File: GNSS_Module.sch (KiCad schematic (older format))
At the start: 10 parts, among them J12 GPS Shield, J13 GPS_Trasnmission_Conn, U9 ublox_SAM-M8Q

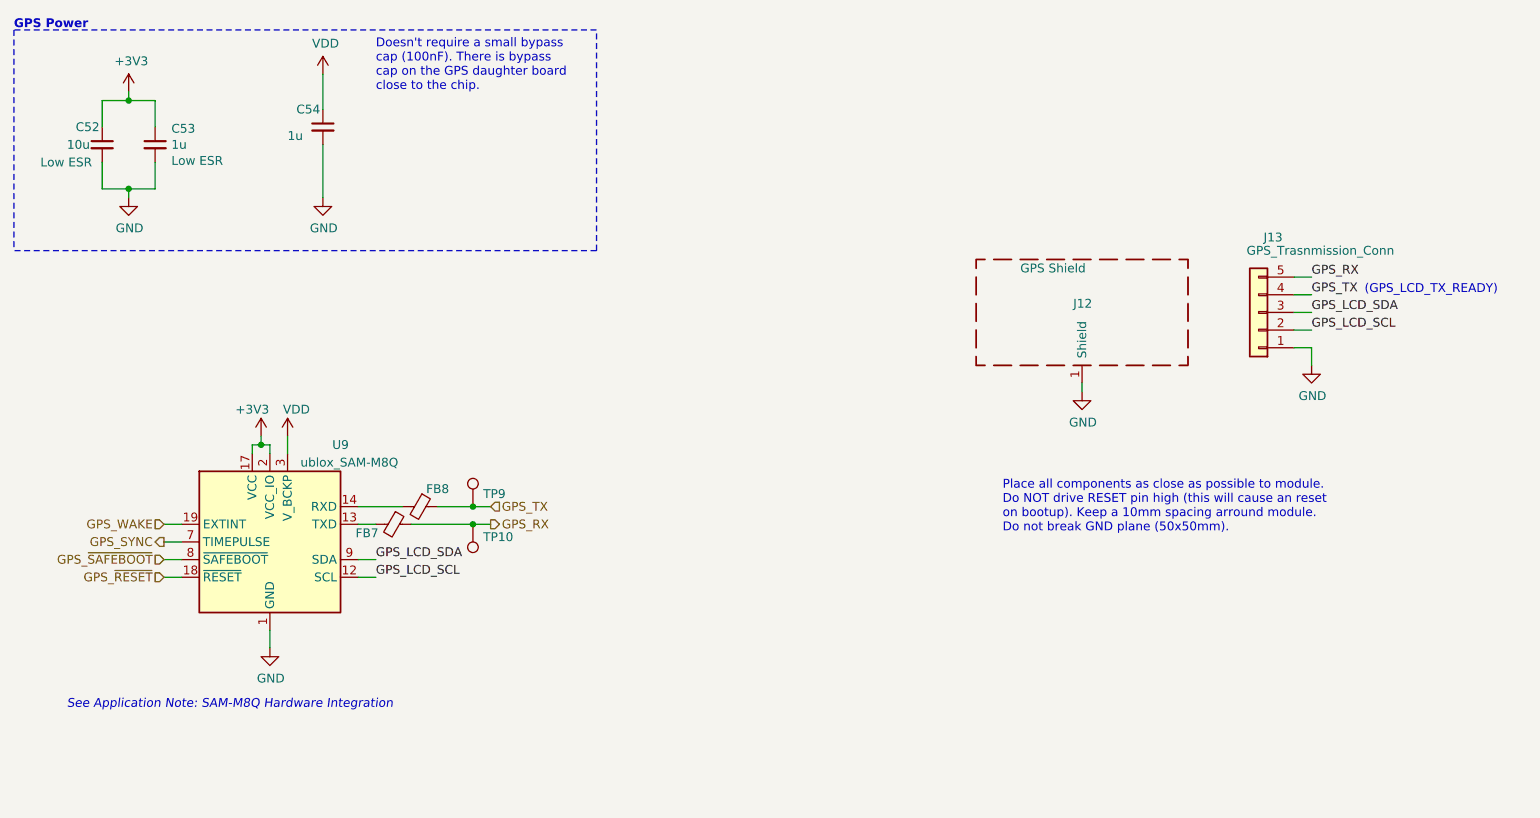
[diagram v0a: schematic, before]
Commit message: Change voltage polarity diode
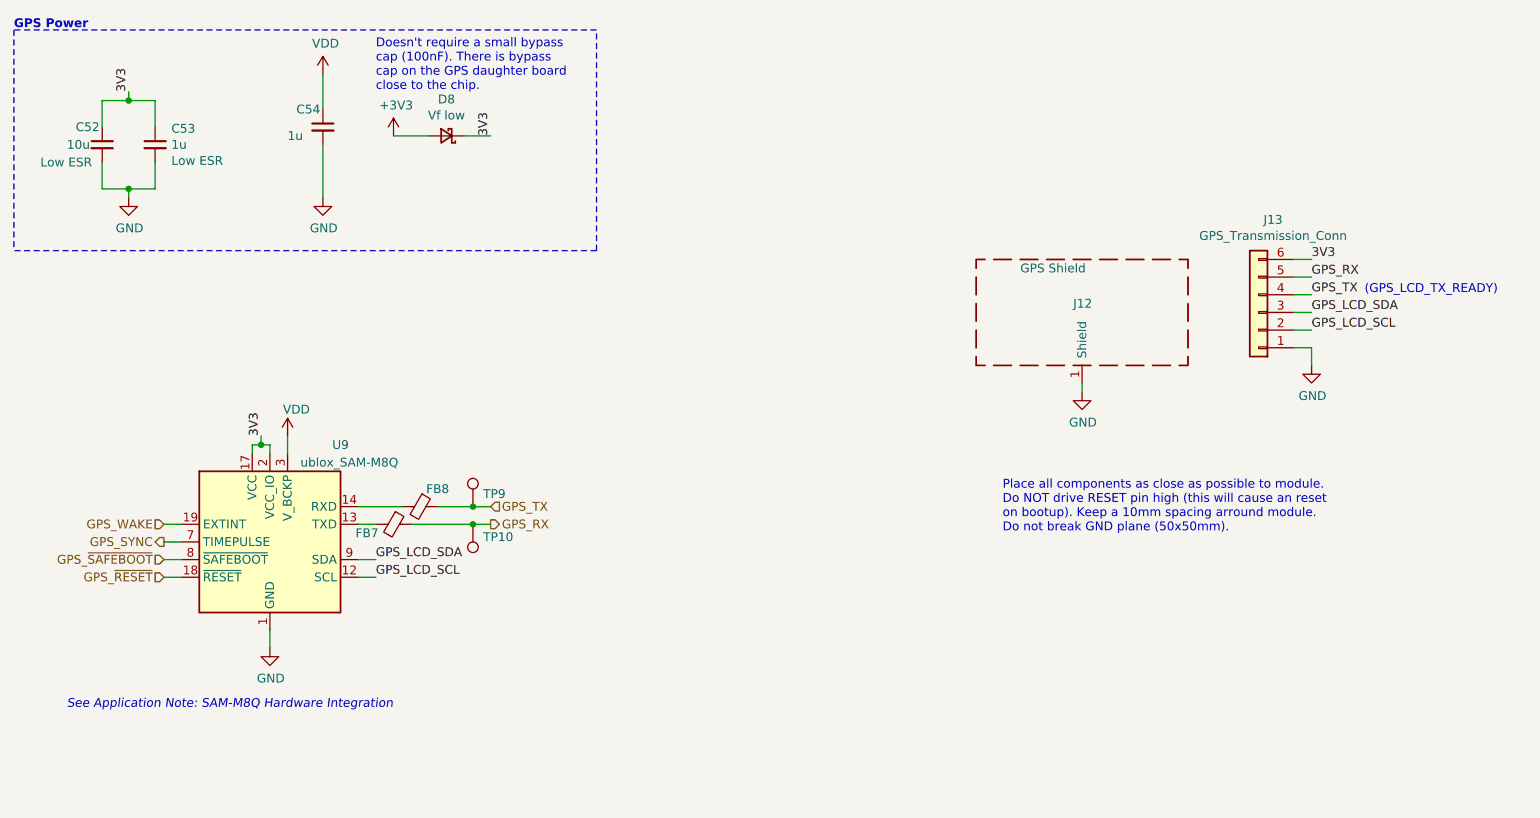
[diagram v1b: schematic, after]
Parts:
- removed J13: GPS_Trasnmission_Conn, Connector_PinHeader_2.54mm:PinHeader_1x05_P2.54mm_Vertical, symbol Connector_Generic:Conn_01x05
- added D8: Vf low, Diode_SMD:D_SOD-123, symbol Device:D_Schottky_Small
- added J13: GPS_Transmission_Conn, Connector_PinHeader_2.54mm:PinHeader_1x06_P2.54mm_Vertical, symbol Connector_Generic:Conn_01x06
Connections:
- net +3V3: now also D8.2 (A); no longer C52.1, C53.1, U9.17 (VCC), U9.2 (VCC_IO)
- net GND: now also J13.1 (Pin_1)
- net GPS_LCD_SCL: now also J13.2 (Pin_2)
- net GPS_LCD_SDA: now also J13.3 (Pin_3)
- net GPS_RX: now also J13.5 (Pin_5)
- net GPS_TX: now also J13.4 (Pin_4)
- new net 3V3: C52.1, C53.1, D8.1 (K), J13.6 (Pin_6), U9.17 (VCC), U9.2 (VCC_IO)
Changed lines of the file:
@@
 	2250 1750 2100 1750
-$Comp
-L power:+3V3 #PWR?
-U 1 1 5EE05208
-P 2250 1200
-AR Path="/5EE05208" Ref="#PWR?"  Part="1"
-AR Path="/5EDF3693/5EE05208" Ref="#PWR0120"  Part="1"
-F 0 "#PWR0120" H 2250 1050 50  0001 C CNN
-F 1 "+3V3" H 2265 1373 50  0000 C CNN
-F 2 "" H 2250 1200 50  0001 C CNN
-F 3 "" H 2250 1200 50  0001 C CNN
-	1    2250 1200
-	1    0    0    -1
-$EndComp
 $Comp
 L power:GND #PWR?
@@
 F 3 "" H 3350 1800 50  0001 C CNN
 	1    3350 1800
-	1    0    0    -1
-$EndComp
-$Comp
-L power:+3V3 #PWR?
-U 1 1 5EE05214
-P 3000 3150
-AR Path="/5EE05214" Ref="#PWR?"  Part="1"
-AR Path="/5EDF3693/5EE05214" Ref="#PWR0122"  Part="1"
-F 0 "#PWR0122" H 3000 3000 50  0001 C CNN
-F 1 "+3V3" H 2950 3300 50  0000 C CNN
-F 2 "" H 3000 3150 50  0001 C CNN
-F 3 "" H 3000 3150 50  0001 C CNN
-	1    3000 3150
 	1    0    0    -1
 $EndComp
@@
 Wire Wire Line
 	3550 3950 3650 3950
-$Comp
-L Connector_Generic:Conn_01x05 J?
-U 1 1 5EE05249
-P 8650 2450
-AR Path="/5EE05249" Ref="J?"  Part="1"
-AR Path="/5EDF3693/5EE05249" Ref="J13"  Part="1"
-F 0 "J13" H 8568 2025 50  0000 C CNN
-F 1 "GPS_Trasnmission_Conn" H 8300 2100 50  0000 C CNN
-F 2 "Connector_PinHeader_2.54mm:PinHeader_1x05_P2.54mm_Vertical" H 8650 2450 50  0001 C CNN
-F 3 "~" H 8650 2450 50  0001 C CNN
-	1    8650 2450
-	-1   0    0    1
-$EndComp
 $Comp
 L power:GND #PWR?
@@
 Wire Wire Line
 	3350 1100 3350 1300
+$Comp
+L Connector_Generic:Conn_01x06 J13
+U 1 1 5EEF6B4C
+P 8650 2450
+F 0 "J13" H 8568 1925 50  0000 C CNN
+F 1 "GPS_Transmission_Conn" H 8568 2016 50  0000 C CNN
+F 2 "Connector_PinHeader_2.54mm:PinHeader_1x06_P2.54mm_Vertical" H 8650 2450 50  0001 C CNN
+F 3 "~" H 8650 2450 50  0001 C CNN
+	1    8650 2450
+	-1   0    0    1
+$EndComp
+Text Label 8950 2150 0    50   ~ 0
+3V3
+Wire Wire Line
+	8950 2150 8850 2150
+Text Label 2250 1200 1    50   ~ 0
+3V3
+Text Label 3000 3150 1    50   ~ 0
+3V3
+Wire Wire Line
+	3950 1450 3750 1450
+Wire Wire Line
+	4300 1450 4150 1450
+Text Label 4300 1450 1    50   ~ 0
+3V3
+$Comp
+L power:+3V3 #PWR0120
+U 1 1 5EF0BA19
+P 3750 1450
+F 0 "#PWR0120" H 3750 1300 50  0001 C CNN
+F 1 "+3V3" H 3765 1623 50  0000 C CNN
+F 2 "" H 3750 1450 50  0001 C CNN
+F 3 "" H 3750 1450 50  0001 C CNN
+	1    3750 1450
+	1    0    0    -1
+$EndComp
+$Comp
+L Device:D_Schottky_Small D?
+U 1 1 5EF05AAC
+P 4050 1450
+AR Path="/5EEDE770/5EF05AAC" Ref="D?"  Part="1"
+AR Path="/5EDF3693/5EF05AAC" Ref="D8"  Part="1"
+F 0 "D8" H 4050 1243 50  0000 C CNN
+F 1 "Vf low" H 4050 1334 50  0000 C CNN
+F 2 "Diode_SMD:D_SOD-123" V 4050 1450 50  0001 C CNN
+F 3 "~" V 4050 1450 50  0001 C CNN
+F 4 "RSX101MM-30TR" H 4050 1450 50  0001 C CNN "MPN"
+F 5 "ROHM Semiconductor" H 4050 1450 50  0001 C CNN "Mfr."
+	1    4050 1450
+	-1   0    0    1
+$EndComp
 $EndSCHEMATC

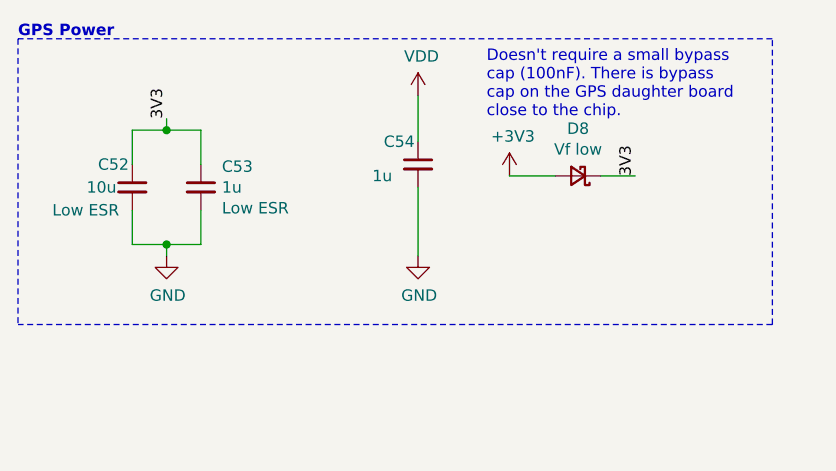
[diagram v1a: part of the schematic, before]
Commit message: Change Mic Preamp
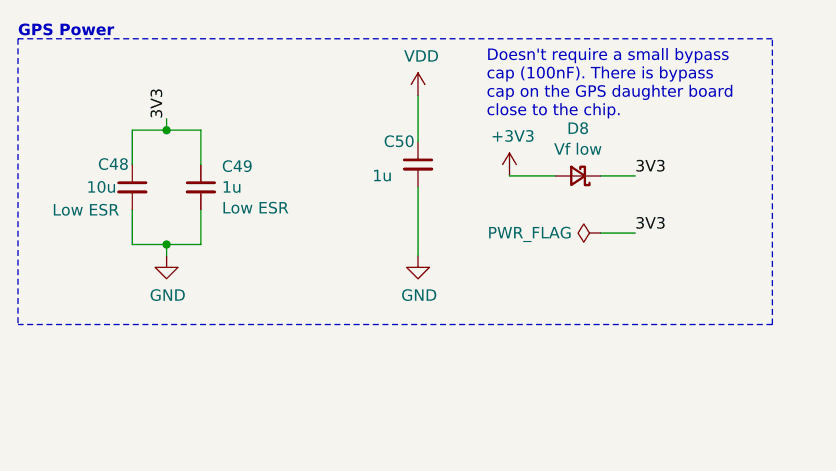
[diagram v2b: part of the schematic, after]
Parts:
- C48: renamed from C52; MPN (none) -> C0805C106K9PACTU; Mfr. (none) -> KEMET
- C50: renamed from C54; MPN (none) -> C0603C105K8RACTU; Mfr. (none) -> KEMET
- FB7, FB8: MPN BLM15HD102SN1 -> BLM15HD102SN1D; Mfr. (none) -> Murata Electronics
- renumbered C53 to C49
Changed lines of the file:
@@
 P 2250 1800
 AR Path="/5EE05200" Ref="#PWR?"  Part="1"
-AR Path="/5EDF3693/5EE05200" Ref="#PWR0121"  Part="1"
-F 0 "#PWR0121" H 2250 1550 50  0001 C CNN
+AR Path="/5EDF3693/5EE05200" Ref="#PWR0128"  Part="1"
+F 0 "#PWR0128" H 2250 1550 50  0001 C CNN
 F 1 "GND" H 2255 1627 50  0000 C CNN
 F 2 "" H 2250 1800 50  0001 C CNN
@@
 P 3350 1800
 AR Path="/5EE0520E" Ref="#PWR?"  Part="1"
-AR Path="/5EDF3693/5EE0520E" Ref="#PWR0126"  Part="1"
-F 0 "#PWR0126" H 3350 1550 50  0001 C CNN
+AR Path="/5EDF3693/5EE0520E" Ref="#PWR0132"  Part="1"
+F 0 "#PWR0132" H 3350 1550 50  0001 C CNN
 F 1 "GND" H 3355 1627 50  0000 C CNN
 F 2 "" H 3350 1800 50  0001 C CNN
@@
 P 3050 4350
 AR Path="/5EE05234" Ref="#PWR?"  Part="1"
-AR Path="/5EDF3693/5EE05234" Ref="#PWR0123"  Part="1"
-F 0 "#PWR0123" H 3050 4100 50  0001 C CNN
+AR Path="/5EDF3693/5EE05234" Ref="#PWR0129"  Part="1"
+F 0 "#PWR0129" H 3050 4100 50  0001 C CNN
 F 1 "GND" H 3055 4177 50  0000 C CNN
 F 2 "" H 3050 4350 50  0001 C CNN
@@
 F 2 "Inductor_SMD:L_0402_1005Metric" V 3680 3650 50  0001 C CNN
 F 3 "~" H 3750 3650 50  0001 C CNN
-F 4 "BLM15HD102SN1" V 3750 3650 50  0001 C CNN "MPN"
+F 4 "BLM15HD102SN1D" V 3750 3650 50  0001 C CNN "MPN"
+F 5 "Murata Electronics" H 3750 3650 50  0001 C CNN "Mfr."
 	1    3750 3650
 	0    1    1    0
@@
 P 8950 2750
 AR Path="/5EE0524F" Ref="#PWR?"  Part="1"
-AR Path="/5EDF3693/5EE0524F" Ref="#PWR0128"  Part="1"
-F 0 "#PWR0128" H 8950 2500 50  0001 C CNN
+AR Path="/5EDF3693/5EE0524F" Ref="#PWR0135"  Part="1"
+F 0 "#PWR0135" H 8950 2500 50  0001 C CNN
 F 1 "GND" H 8955 2577 50  0000 C CNN
 F 2 "" H 8950 2750 50  0001 C CNN
@@
 P 2400 1500
 AR Path="/5EE0527F" Ref="C?"  Part="1"
-AR Path="/5EDF3693/5EE0527F" Ref="C53"  Part="1"
-F 0 "C53" H 2492 1591 50  0000 L CNN
+AR Path="/5EDF3693/5EE0527F" Ref="C49"  Part="1"
+F 0 "C49" H 2492 1591 50  0000 L CNN
 F 1 "1u" H 2492 1500 50  0000 L CNN
 F 2 "Capacitor_SMD:C_0603_1608Metric_Pad1.05x0.95mm_HandSolder" H 2400 1500 50  0001 C CNN
@@
 P 3350 1400
 AR Path="/5EE05285" Ref="C?"  Part="1"
-AR Path="/5EDF3693/5EE05285" Ref="C54"  Part="1"
-F 0 "C54" H 3200 1500 50  0000 L CNN
+AR Path="/5EDF3693/5EE05285" Ref="C50"  Part="1"
+F 0 "C50" H 3200 1500 50  0000 L CNN
 F 1 "1u" H 3150 1350 50  0000 L CNN
 F 2 "Capacitor_SMD:C_0603_1608Metric_Pad1.05x0.95mm_HandSolder" H 3350 1400 50  0001 C CNN
 F 3 "~" H 3350 1400 50  0001 C CNN
+F 4 "C0603C105K8RACTU" H 3350 1400 50  0001 C CNN "MPN"
+F 5 "KEMET" H 3350 1400 50  0001 C CNN "Mfr."
 	1    3350 1400
 	1    0    0    -1
@@
 P 2100 1500
 AR Path="/5EE0528E" Ref="C?"  Part="1"
-AR Path="/5EDF3693/5EE0528E" Ref="C52"  Part="1"
-F 0 "C52" H 1950 1600 50  0000 L CNN
+AR Path="/5EDF3693/5EE0528E" Ref="C48"  Part="1"
+F 0 "C48" H 1950 1600 50  0000 L CNN
 F 1 "10u" H 1900 1500 50  0000 L CNN
 F 2 "Capacitor_SMD:C_0805_2012Metric_Pad1.15x1.40mm_HandSolder" H 2100 1500 50  0001 C CNN
 F 3 "~" H 2100 1500 50  0001 C CNN
 F 4 "Low ESR" H 1750 1400 50  0000 L CNN "Notes"
+F 5 "C0805C106K9PACTU" H 2100 1500 50  0001 C CNN "MPN"
+F 6 "KEMET" H 2100 1500 50  0001 C CNN "Mfr."
 	1    2100 1500
 	1    0    0    -1
@@
 P 7650 2900
 AR Path="/5EE052A0" Ref="#PWR?"  Part="1"
-AR Path="/5EDF3693/5EE052A0" Ref="#PWR0127"  Part="1"
-F 0 "#PWR0127" H 7650 2650 50  0001 C CNN
+AR Path="/5EDF3693/5EE052A0" Ref="#PWR0134"  Part="1"
+F 0 "#PWR0134" H 7650 2650 50  0001 C CNN
 F 1 "GND" H 7655 2727 50  0000 C CNN
 F 2 "" H 7650 2900 50  0001 C CNN
@@
 P 3350 1100
 AR Path="/5EE052A8" Ref="#PWR?"  Part="1"
-AR Path="/5EDF3693/5EE052A8" Ref="#PWR0125"  Part="1"
-F 0 "#PWR0125" H 3350 950 50  0001 C CNN
+AR Path="/5EDF3693/5EE052A8" Ref="#PWR0131"  Part="1"
+F 0 "#PWR0131" H 3350 950 50  0001 C CNN
 F 1 "VDD" H 3365 1273 50  0000 C CNN
 F 2 "" H 3350 1100 50  0001 C CNN
@@
 P 3150 3150
 AR Path="/5EE052B2" Ref="#PWR?"  Part="1"
-AR Path="/5EDF3693/5EE052B2" Ref="#PWR0124"  Part="1"
-F 0 "#PWR0124" H 3150 3000 50  0001 C CNN
+AR Path="/5EDF3693/5EE052B2" Ref="#PWR0130"  Part="1"
+F 0 "#PWR0130" H 3150 3000 50  0001 C CNN
 F 1 "VDD" H 3200 3300 50  0000 C CNN
 F 2 "" H 3150 3150 50  0001 C CNN
@@
 F 2 "Inductor_SMD:L_0402_1005Metric" V 3830 3550 50  0001 C CNN
 F 3 "~" H 3900 3550 50  0001 C CNN
-F 4 "BLM15HD102SN1" V 3900 3550 50  0001 C CNN "MPN"
+F 4 "BLM15HD102SN1D" V 3900 3550 50  0001 C CNN "MPN"
+F 5 "Murata Electronics" H 3900 3550 50  0001 C CNN "Mfr."
 	1    3900 3550
 	0    1    1    0
@@
 Wire Wire Line
 	4300 1450 4150 1450
-Text Label 4300 1450 1    50   ~ 0
-3V3
-$Comp
-L power:+3V3 #PWR0120
+Text Label 4300 1450 0    50   ~ 0
+3V3
+$Comp
+L power:+3V3 #PWR0133
 U 1 1 5EF0BA19
 P 3750 1450
-F 0 "#PWR0120" H 3750 1300 50  0001 C CNN
+F 0 "#PWR0133" H 3750 1300 50  0001 C CNN
 F 1 "+3V3" H 3765 1623 50  0000 C CNN
 F 2 "" H 3750 1450 50  0001 C CNN
@@
 	-1   0    0    1
 $EndComp
+$Comp
+L power:PWR_FLAG #FLG010
+U 1 1 5EF35E8F
+P 4150 1700
+F 0 "#FLG010" H 4150 1775 50  0001 C CNN
+F 1 "PWR_FLAG" V 4150 1827 50  0000 L CNN
+F 2 "" H 4150 1700 50  0001 C CNN
+F 3 "~" H 4150 1700 50  0001 C CNN
+	1    4150 1700
+	0    -1   -1   0
+$EndComp
+Text Label 4300 1700 0    50   ~ 0
+3V3
+Wire Wire Line
+	4300 1700 4150 1700
 $EndSCHEMATC

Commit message: Fix BOM ref
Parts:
- J13: MPN (none) -> M50-055023W0445; Mfr. (none) -> Harwin
- U9: MPN (none) -> SAM-M8Q; Mfr. (none) -> U-BLOX
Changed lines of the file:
@@
 $Descr A4 11693 8268
 encoding utf-8
-Sheet 15 15
+Sheet 17 17
 Title "Kleinvoet"
 Date "2020-06-11"
@@
 F 2 "RF_GPS:ublox_SAM-M8Q" H 3550 3300 50  0001 C CNN
 F 3 "https://www.u-blox.com/sites/default/files/SAM-M8Q_DataSheet_%28UBX-16012619%29.pdf" H 3050 3750 50  0001 C CNN
+F 4 "SAM-M8Q" H 3050 3750 50  0001 C CNN "MPN"
+F 5 "U-BLOX" H 3050 3750 50  0001 C CNN "Mfr."
 	1    3050 3750
 	1    0    0    -1
@@
 F 2 "Connector_PinHeader_2.54mm:PinHeader_1x06_P2.54mm_Vertical" H 8650 2450 50  0001 C CNN
 F 3 "~" H 8650 2450 50  0001 C CNN
+F 4 "M50-055023W0445" H 8650 2450 50  0001 C CNN "MPN"
+F 5 "Harwin" H 8650 2450 50  0001 C CNN "Mfr."
 	1    8650 2450
 	-1   0    0    1

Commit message: Change Sensor Connectors
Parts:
- J12: footprint RF_Shielding:Wuerth_36503505_50x50mm -> RF_Shielding:Wuerth_36103505_50x50mm
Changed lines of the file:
@@
 F 0 "J12" H 7600 2500 50  0000 L CNN
 F 1 "GPS Shield" H 7300 2700 50  0000 L CNN
-F 2 "RF_Shielding:Wuerth_36503505_50x50mm" H 7650 2350 50  0001 C CNN
+F 2 "RF_Shielding:Wuerth_36103505_50x50mm" H 7650 2350 50  0001 C CNN
 F 3 "~" H 7650 2350 50  0001 C CNN
 	1    7650 2450

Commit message: PCB Layout Checkpoint
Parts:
- removed D8: Vf low, Diode_SMD:D_SOD-123, symbol Device:D_Schottky_Small
- removed FB7: BLM15HD102SN1, Inductor_SMD:L_0402_1005Metric, symbol Device:Ferrite_Bead_Small
- removed TP10, TP9: TestPoint, TestPoint:TestPoint_Pad_D1.0mm, symbol Connector:TestPoint
- added CB40: 100n, Capacitor_SMD:C_0603_1608Metric_Pad1.05x0.95mm_HandSolder, symbol Device:C_Small
- U11: renamed from U9; footprint RF_GPS:ublox_SAM-M8Q -> grootvoet:ublox_SAM-M8Q_HandSolder
- renumbered C48 to C64, C49 to C65, C50 to C66, FB8 to FB10, J12 to J14, J13 to J15
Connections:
- net 3V3 is gone; now on net +3V3: C64.1, C65.1, J15.6 (Pin_6), U11.17 (VCC), U11.2 (VCC_IO)
- net GND: now also CB40.2
- net GPS_LCD_SCL: now also J15.4 (Pin_4); no longer J15.2 (Pin_2)
- net GPS_LCD_SDA: now also J15.5 (Pin_5); no longer J15.3 (Pin_3)
- net GPS_RX: now also J15.3 (Pin_3), U11.13 (TXD); no longer J15.5 (Pin_5)
- net GPS_TX: now also J15.2 (Pin_2); no longer J15.4 (Pin_4)
- net GPS_~RESET: now also CB40.1

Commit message: Major Commit with Final PCB Design
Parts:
- removed J14: GPS Shield, RF_Shielding:Wuerth_36103505_50x50mm, symbol Device:RF_Shield_One_Piece
- removed J15: GPS_Transmission_Conn, Connector_PinHeader_2.54mm:PinHeader_1x06_P2.54mm_Vertical, symbol Connector_Generic:Conn_01x06
- added D2: GREEN, LED_SMD:LED_0603_1608Metric_Pad1.05x0.95mm_HandSolder, symbol Device:LED_Small
- added D3: YELLOW, LED_SMD:LED_0603_1608Metric_Pad1.05x0.95mm_HandSolder, symbol Device:LED_Small
- added H13, H14, H15, H16: MountingHole_Pad, MountingHole:MountingHole_4.3mm_M4_Pad_Via, symbol Mechanical:MountingHole_Pad
- added J14: GPS_Transmission_Conn, Connector_PinHeader_1.27mm:PinHeader_1x08_P1.27mm_Vertical, symbol Connector_Generic:Conn_01x08
- added J16: GPS_Transmission_Conn, Connector_PinHeader_1.27mm:PinHeader_2x04_P1.27mm_Vertical, symbol Connector_Generic:Conn_02x04_Odd_Even
- added J2: FTDI_Conn, Connector_PinHeader_2.54mm:PinHeader_1x06_P2.54mm_Vertical, symbol Connector_Generic:Conn_01x06
- added R3, R4: 2.2k, Resistor_SMD:R_0603_1608Metric_Pad1.05x0.95mm_HandSolder, symbol Device:R_Small
- C65: value 1u -> 10u; footprint Capacitor_SMD:C_0603_1608Metric_Pad1.05x0.95mm_HandSolder -> Capacitor_SMD:C_0805_2012Metric_Pad1.15x1.40mm_HandSolder; MPN C0603C105K8RACTU -> C0805C106K9PACTU
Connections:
- net +3V3: now also J14.8 (Pin_8), J16.6 (Pin_6), J2.3 (Pin_3), R3.1, R4.1
- net GND: now also J14.7 (Pin_7), J16.4 (Pin_4), J2.1 (Pin_1)
- net GPS_RX: now also D2.1 (K), J14.4 (Pin_4), J16.5 (Pin_5), J2.5 (Pin_5)
- net GPS_SYNC: now also J14.6 (Pin_6), J16.7 (Pin_7)
- net GPS_TX: now also D3.1 (K), J14.3 (Pin_3), J16.3 (Pin_3), J2.4 (Pin_4)
- net GPS_WAKE: now also J14.2 (Pin_2), J16.8 (Pin_8)
- net GPS_~RESET: now also J14.1 (Pin_1), J16.1 (Pin_1)
- net GPS_~SAFEBOOT: now also J14.5 (Pin_5), J16.2 (Pin_2)
- net GPS_LCD_SCL: no longer names the net of U11.12 (SCL)
- net GPS_LCD_SDA: no longer names the net of U11.9 (SDA)
- new net: D2.2 (A), R3.2
- new net: D3.2 (A), R4.2
- new net Earth: H13.1, H14.1, H15.1, H16.1
- no-connect marks 0 -> 4
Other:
- note removed: "(GPS_LCD_TX_READY)"

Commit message: CHange to single 3 designs to save cost
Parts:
- H13, H14, H15, H16: footprint MountingHole:MountingHole_4.3mm_M4_Pad_Via -> MountingHole:MountingHole_3.2mm_M3_Pad_Via
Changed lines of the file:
@@
 F 0 "H16" H 8200 3003 50  0000 L CNN
 F 1 "MountingHole_Pad" H 8200 2958 50  0001 L CNN
-F 2 "MountingHole:MountingHole_4.3mm_M4_Pad_Via" H 8100 3000 50  0001 C CNN
+F 2 "MountingHole:MountingHole_3.2mm_M3_Pad_Via" H 8100 3000 50  0001 C CNN
 F 3 "~" H 8100 3000 50  0001 C CNN
 	1    8100 3000
@@
 F 0 "H15" H 7900 3003 50  0000 L CNN
 F 1 "MountingHole_Pad" H 7900 2958 50  0001 L CNN
-F 2 "MountingHole:MountingHole_4.3mm_M4_Pad_Via" H 7800 3000 50  0001 C CNN
+F 2 "MountingHole:MountingHole_3.2mm_M3_Pad_Via" H 7800 3000 50  0001 C CNN
 F 3 "~" H 7800 3000 50  0001 C CNN
 	1    7800 3000
@@
 F 0 "H14" H 7600 3003 50  0000 L CNN
 F 1 "MountingHole_Pad" H 7600 2958 50  0001 L CNN
-F 2 "MountingHole:MountingHole_4.3mm_M4_Pad_Via" H 7500 3000 50  0001 C CNN
+F 2 "MountingHole:MountingHole_3.2mm_M3_Pad_Via" H 7500 3000 50  0001 C CNN
 F 3 "~" H 7500 3000 50  0001 C CNN
 	1    7500 3000
@@
 F 0 "H13" H 7300 3003 50  0000 L CNN
 F 1 "MountingHole_Pad" H 7300 2958 50  0001 L CNN
-F 2 "MountingHole:MountingHole_4.3mm_M4_Pad_Via" H 7200 3000 50  0001 C CNN
+F 2 "MountingHole:MountingHole_3.2mm_M3_Pad_Via" H 7200 3000 50  0001 C CNN
 F 3 "~" H 7200 3000 50  0001 C CNN
 	1    7200 3000
